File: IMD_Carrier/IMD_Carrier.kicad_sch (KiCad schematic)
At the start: 48 parts, among them J1 JST-XA, J2 JST-XA, J3 MicroFit+, J4 MicroFit+, Q2 BSS205N, Q3 BSS205N, U1 TLV1702, U2 BD450, U3 CD4043BE, U4 LMR50410-3.3V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

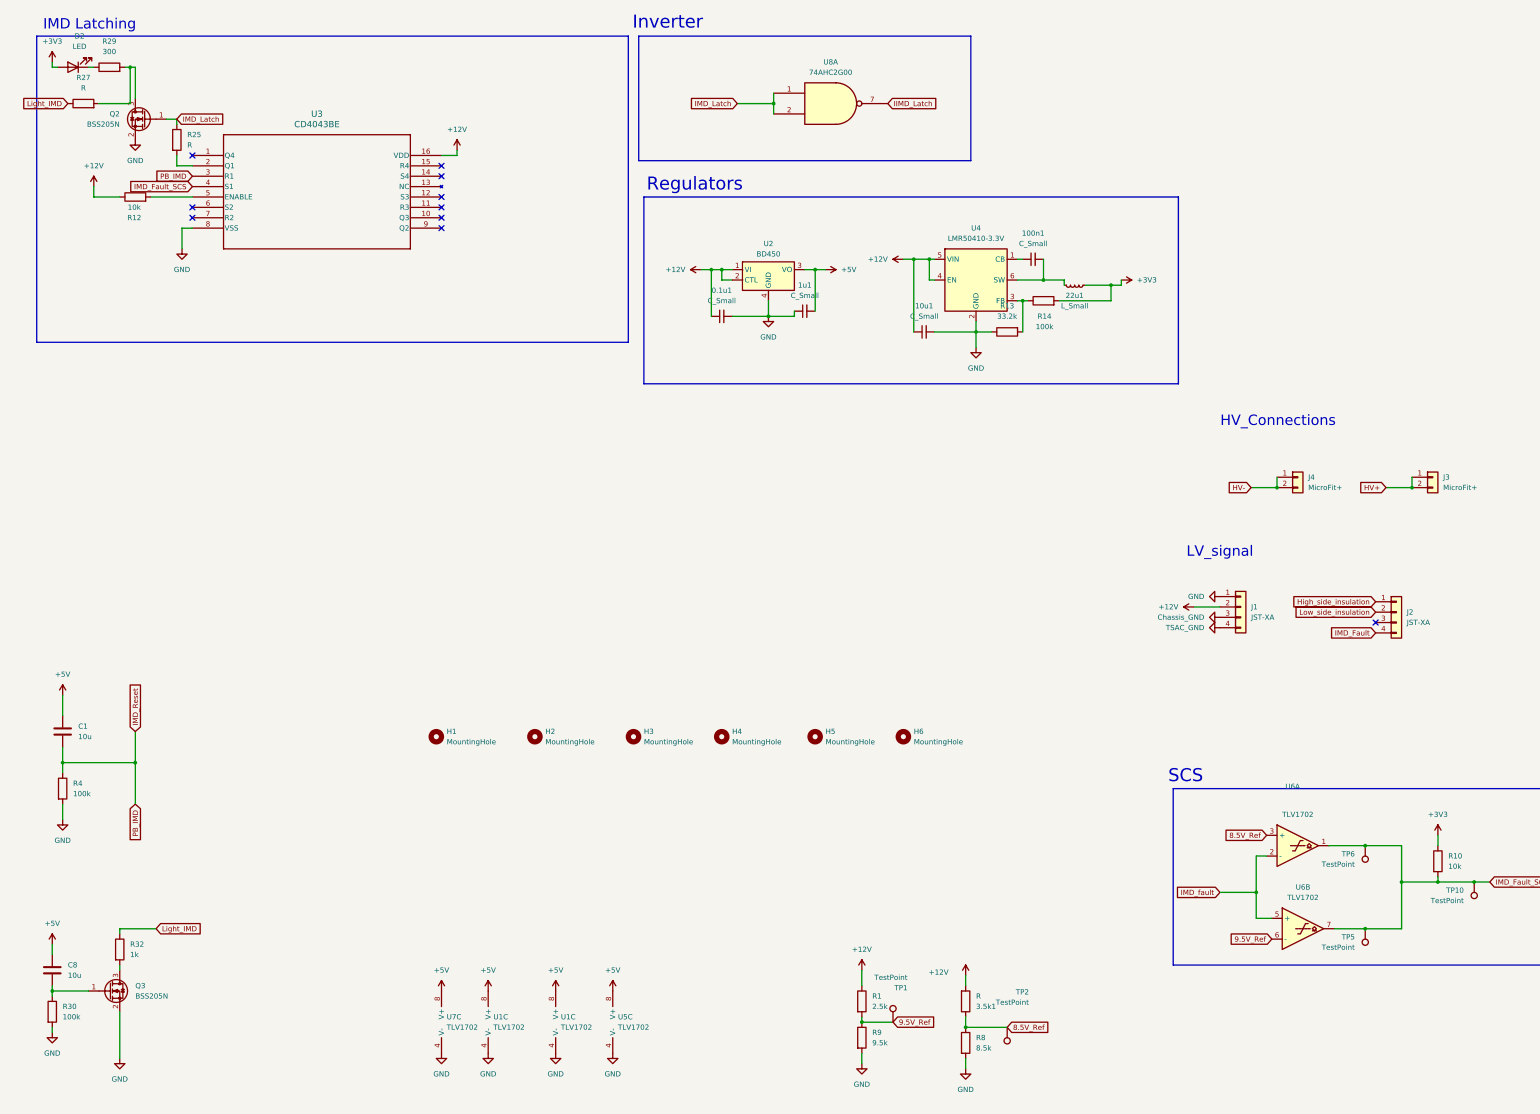
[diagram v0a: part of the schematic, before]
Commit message: Fully finished schematic+partial routing
-Removed the need for regulators by changing all logic to 12V
-Current Calculations for power connections still need to be done
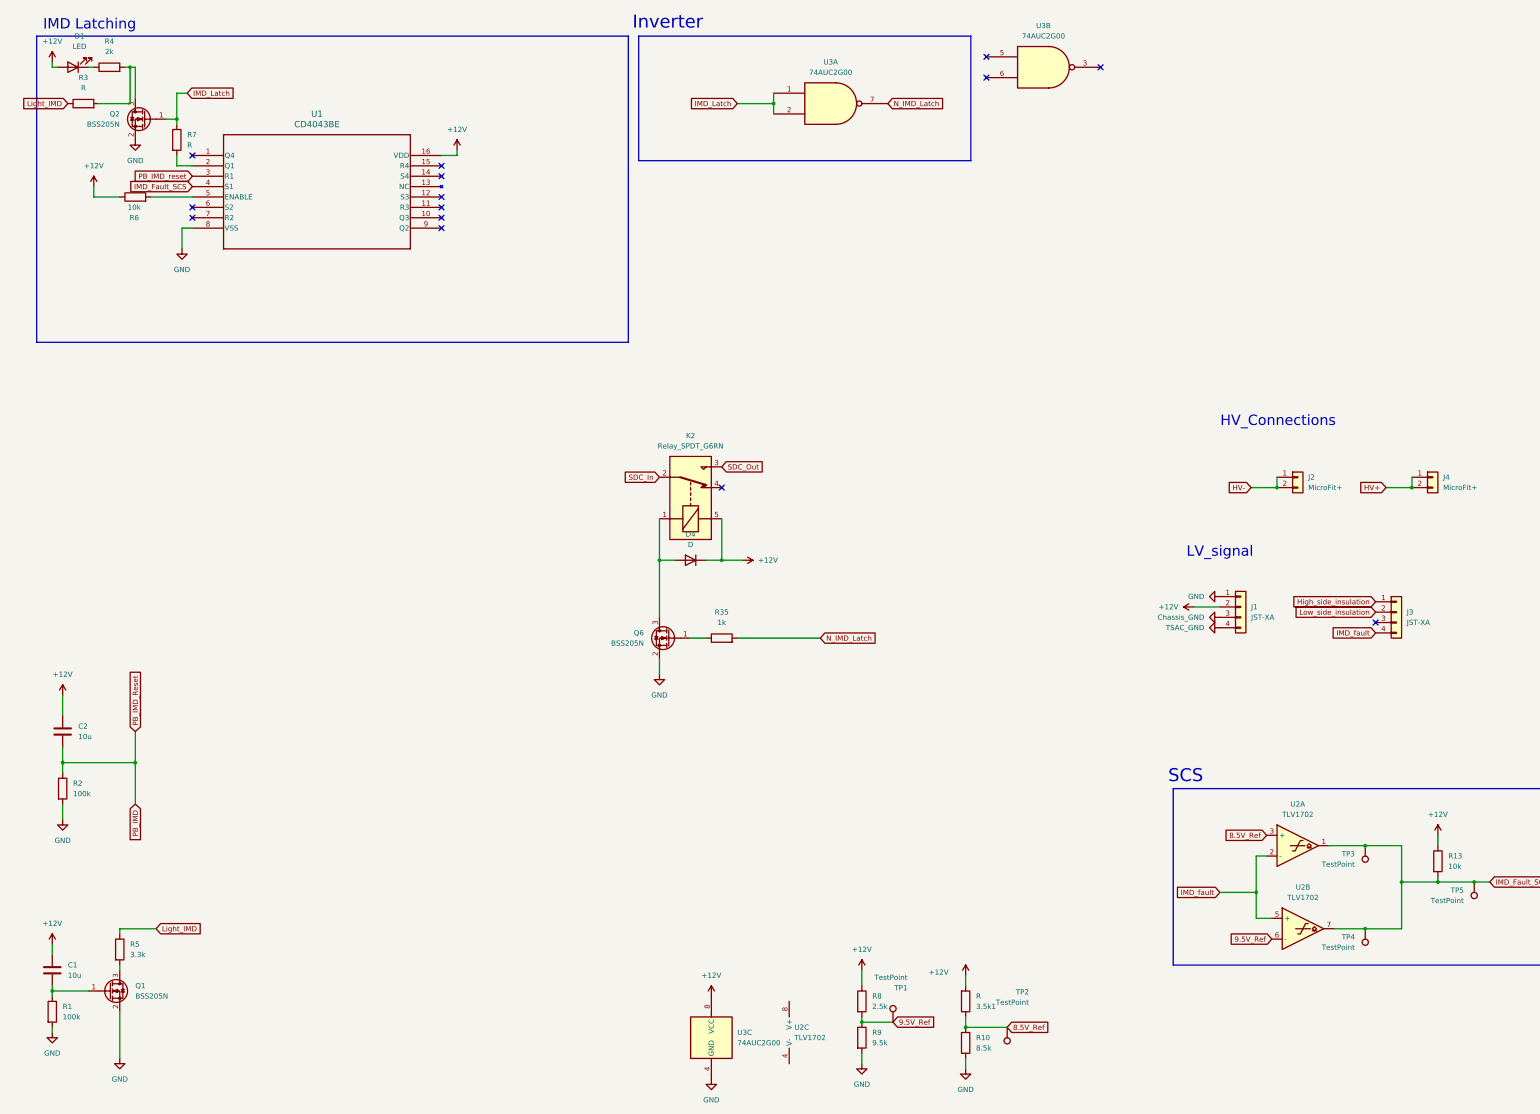
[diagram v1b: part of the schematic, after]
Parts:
- removed 0.1u1, 100n1, 10u1, 1u1: C_Small, Capacitor_SMD:C_0603_1608Metric, symbol Device:C_Small
- removed 22u1: L_Small, Inductor_SMD:L_0603_1608Metric, symbol Device:L_Small
- removed H1, H2, H3, H4, H5, H6: MountingHole, symbol Mechanical:MountingHole
- removed R13: 33.2k, Resistor_SMD:R_0603_1608Metric, symbol Device:R
- removed R14: 100k, Resistor_SMD:R_0603_1608Metric, symbol Device:R
- removed U1 (x2), U5, U6, U7: TLV1702, Custom_MSM:Comparator_Dual_VSSOP-8, symbol Custom_MSM:Comparator_Dual_Open-Coll
- removed U2: BD450, Custom_MSM:Regulator_Linear_SOT-223-4, symbol Custom_MSM1:Regulator_Linear_5V
- removed U4: LMR50410-3.3V, Package_SO:SOIC-8_3.9x4.9mm_P1.27mm, symbol Custom_MSM:Regulator_Switching_3.3V
- removed U8: 74AHC2G00, Custom_MSM:74AHC2G00DC-Q100, symbol 74xGxx:74AHC2G00
- added D4: D, Diode_SMD:D_0805_2012Metric, symbol Device:D
- added K2: Relay_SPDT_G6RN, Custom_MSM:Relay_SPDT_G6RN, symbol Custom_MSM:Relay_SPDT_G6RN
- added Q6: BSS205N, Custom_MSM:MOSFET_Single_SOT-23, symbol Custom_MSM:MOSFET_N-CH
- added R35: 1k, Resistor_SMD:R_0805_2012Metric, symbol Device:R
- added U2: TLV1702, Custom_MSM:Comparator_Dual_VSSOP-8, symbol Custom_MSM1:Comparator_Dual_Open-Coll
- added U3: 74AUC2G00, Custom_MSM:74AHC2G00DC-Q100, symbol 74xGxx:74AUC2G00
- 3.5k1, R9: footprint Resistor_SMD:R_0603_1608Metric -> Resistor_SMD:R_0805_2012Metric
- C1: renamed from C8; footprint Capacitor_SMD:C_0603_1608Metric -> Capacitor_SMD:C_0805_2012Metric
- C2: renamed from C1; footprint Capacitor_SMD:C_0603_1608Metric -> Capacitor_SMD:C_0805_2012Metric
- D1: renamed from D2; footprint LED_SMD:LED_0603_1608Metric -> LED_SMD:LED_0805_2012Metric
- R1: renamed from R30; footprint Resistor_SMD:R_0603_1608Metric -> Resistor_SMD:R_0805_2012Metric
- R10: renamed from R8; footprint Resistor_SMD:R_0603_1608Metric -> Resistor_SMD:R_0805_2012Metric
- R13: renamed from R10; footprint Resistor_SMD:R_0603_1608Metric -> Resistor_SMD:R_0805_2012Metric
- R2: renamed from R4; footprint Resistor_SMD:R_0603_1608Metric -> Resistor_SMD:R_0805_2012Metric
- R3: renamed from R27; footprint Resistor_SMD:R_0603_1608Metric -> Resistor_SMD:R_0805_2012Metric
- R4: renamed from R29; value 300 -> 2k; footprint Resistor_SMD:R_0603_1608Metric -> Resistor_SMD:R_0805_2012Metric
- R5: renamed from R32; value 1k -> 3.3k; footprint Resistor_SMD:R_0603_1608Metric -> Resistor_SMD:R_0805_2012Metric
- R6: renamed from R12; footprint Resistor_SMD:R_0603_1608Metric -> Resistor_SMD:R_0805_2012Metric
- R7: renamed from R25; footprint Resistor_SMD:R_0603_1608Metric -> Resistor_SMD:R_0805_2012Metric
- R8: renamed from R1; footprint Resistor_SMD:R_0603_1608Metric -> Resistor_SMD:R_0805_2012Metric
- TP1, TP2: footprint Capacitor_SMD:C_0603_1608Metric_Pad1.08x0.95mm_HandSolder -> TestPoint:TestPoint_Pad_1.0x1.0mm
- TP3: renamed from TP6; footprint Capacitor_SMD:C_0603_1608Metric_Pad1.08x0.95mm_HandSolder -> TestPoint:TestPoint_Pad_1.0x1.0mm
- TP4: renamed from TP5; footprint Capacitor_SMD:C_0603_1608Metric_Pad1.08x0.95mm_HandSolder -> TestPoint:TestPoint_Pad_1.0x1.0mm
- TP5: renamed from TP10; footprint Capacitor_SMD:C_0603_1608Metric_Pad1.08x0.95mm_HandSolder -> TestPoint:TestPoint_Pad_1.0x1.0mm
- renumbered J4 to J2, J2 to J3, J3 to J4, Q3 to Q1, U3 to U1
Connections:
- net +3V3 is gone; now on net +12V: D1.2 (A), R13.1
- net +5V is gone; now on net +12V: C1.1, C2.1
- net IMD_Fault is gone; now on net IMD_fault: J3.4 (Pin_4)
- net +12V: now also D4.1 (K), K2.5, U3.8 (VCC)
- net 8.5V_Ref: now also U2.3 (+)
- net 9.5V_Ref: now also U2.6 (-)
- net GND: now also Q6.2 (S), U3.4 (GND)
- net IMD_Fault_SCS: now also U2.1, U2.7
- net IMD_Latch: now also U3.1, U3.2
- net IMD_fault: now also U2.2 (-), U2.5 (+)
- net IMD_Reset renamed PB_IMD
- net PB_IMD: no longer U1.3 (R1)
- new net: D4.2 (A), K2.1, Q6.3 (D)
- new net: Q6.1 (G), R35.1
- new net N_IMD_Latch: R35.2, U3.7
- new net PB_IMD_reset: U1.3 (R1)
- new net SDC_In: K2.2
- new net SDC_Out: K2.3
- no-connect marks 10 -> 14
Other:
- note removed: "Regulators"

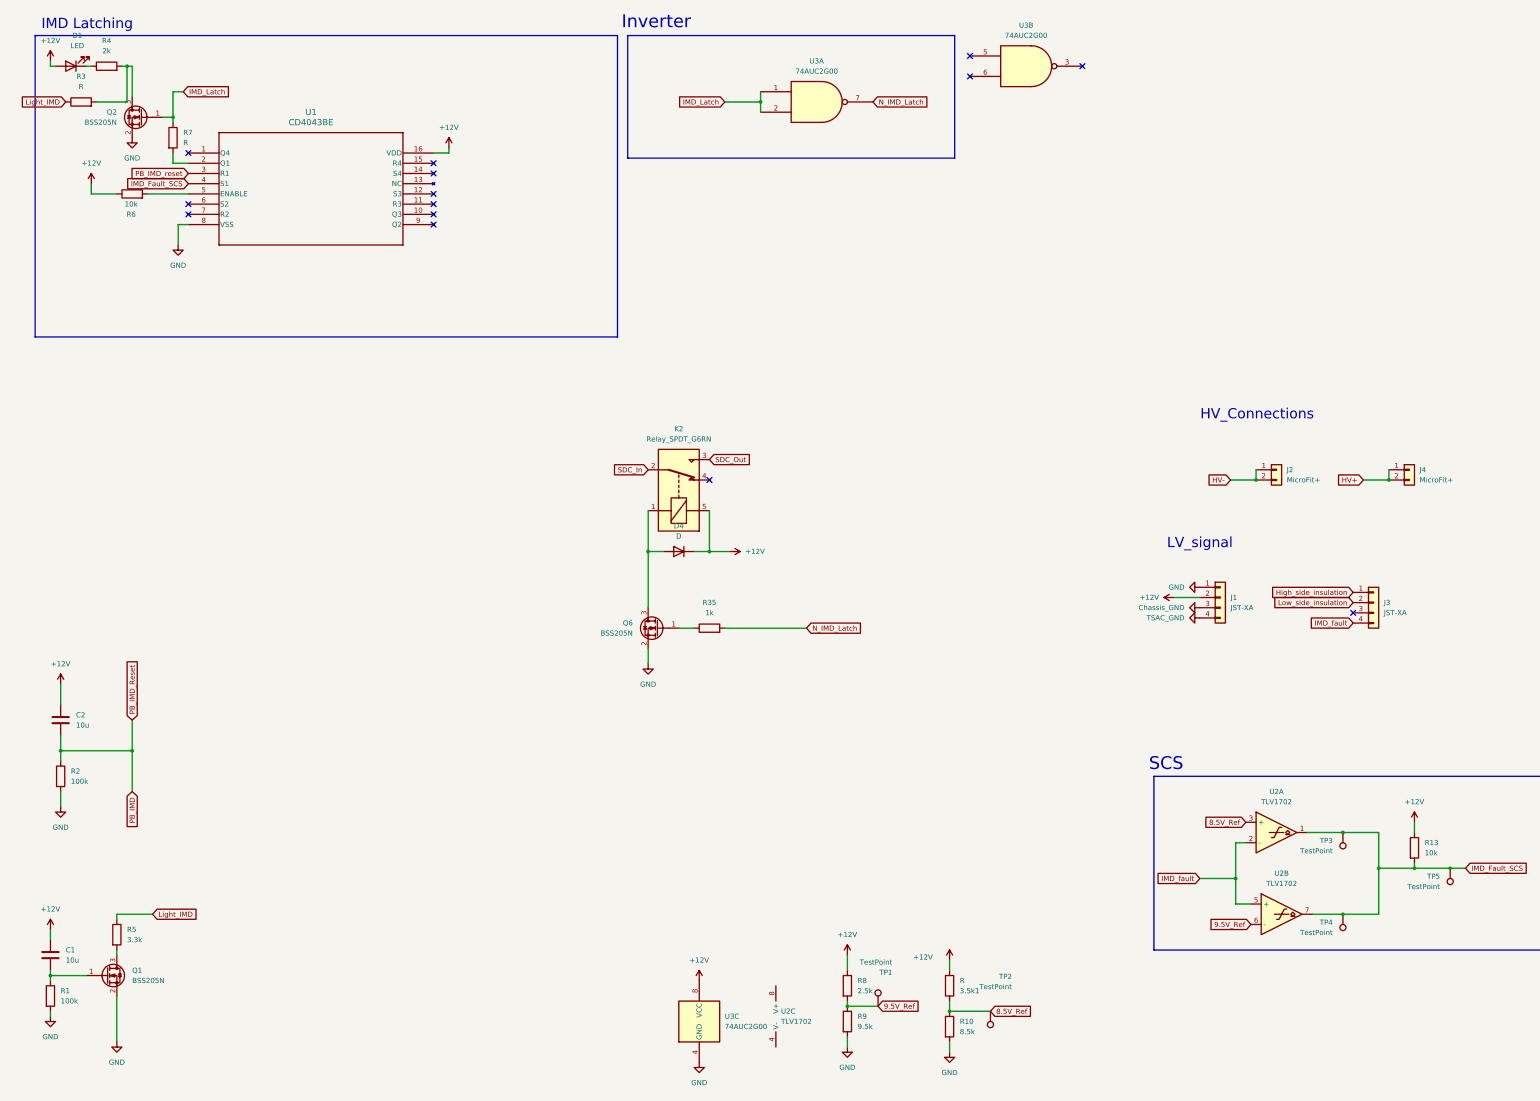
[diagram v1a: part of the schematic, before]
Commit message: finished the routing of the PCB (to be checked)
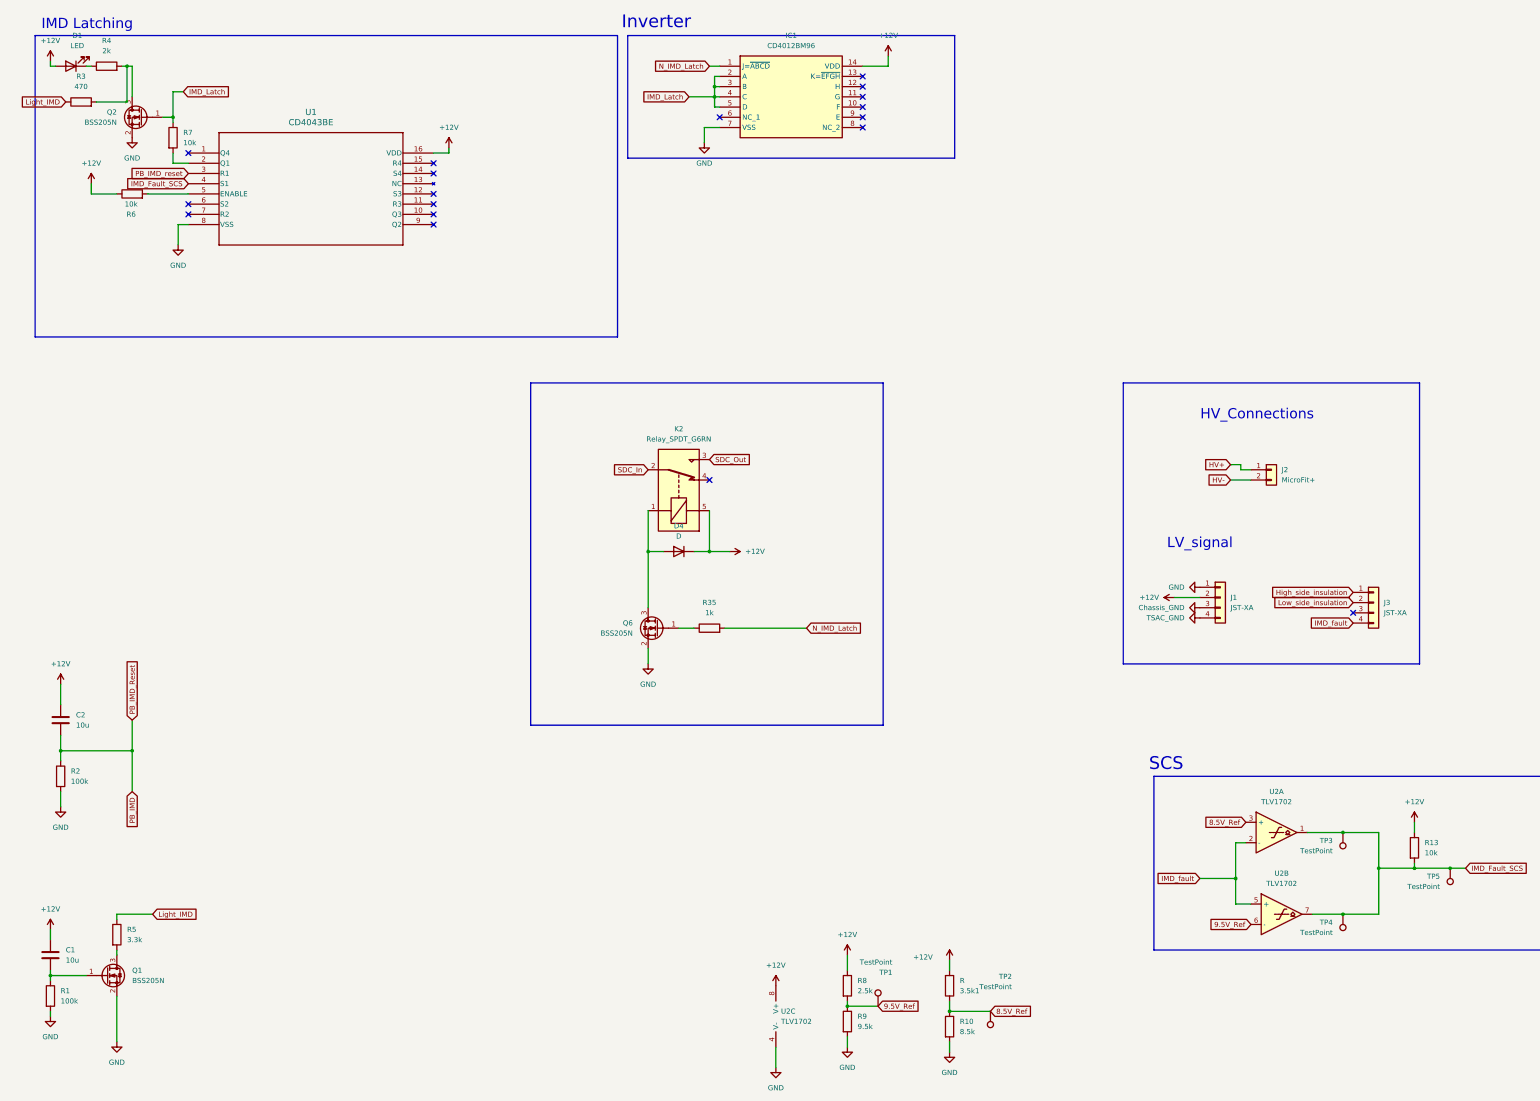
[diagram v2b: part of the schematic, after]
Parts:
- removed J4: MicroFit+, Custom_MSM:Connector_MicroFit-Plus_2POS, symbol Custom_MSM1:Connector_MicroFit-Plus_2POS
- removed U3: 74AUC2G00, Custom_MSM:74AHC2G00DC-Q100, symbol 74xGxx:74AUC2G00
- added IC1: CD4012BM96, Custom_MSM:Dual NAND, Quad input, symbol CD4012BM96:CD4012BM96
- R3: value R -> 470
- R7: value R -> 10k
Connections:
- net +12V: now also U2.8 (V+), IC1.14 (VDD)
- net GND: now also U2.4 (V-), IC1.7 (VSS)
- net HV+: now also J2.1 (Pin_1)
- net HV-: no longer J2.1 (Pin_1)
- net IMD_Latch: now also IC1.2 (A), IC1.3 (B), IC1.4 (C), IC1.5 (D)
- net N_IMD_Latch: now also IC1.1 (J=~{ABCD})
- no-connect marks 14 -> 18
